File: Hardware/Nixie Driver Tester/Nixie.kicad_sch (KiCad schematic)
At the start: 3 parts, among them J4 Conn_01x04, J5 Conn_01x03, J6 Conn_01x03

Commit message: Initial component layout.
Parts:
- J4: footprint (none) -> Connector_PinHeader_2.54mm:PinHeader_1x04_P2.54mm_Vertical
- J5, J6: footprint (none) -> Connector_PinHeader_2.54mm:PinHeader_1x03_P2.54mm_Vertical
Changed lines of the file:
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@@
 			)
 		)
-		(property "Footprint" ""
+		(property "Footprint" "Connector_PinHeader_2.54mm:PinHeader_1x04_P2.54mm_Vertical"
 			(at 151.13 109.22 0)
 			(effects
@@
 			)
 		)
-		(property "Footprint" ""
+		(property "Footprint" "Connector_PinHeader_2.54mm:PinHeader_1x03_P2.54mm_Vertical"
 			(at 144.78 101.6 0)
 			(effects
@@
 			)
 		)
-		(property "Footprint" ""
+		(property "Footprint" "Connector_PinHeader_2.54mm:PinHeader_1x03_P2.54mm_Vertical"
 			(at 160.02 101.6 0)
 			(effects

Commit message: First reasonable layout.
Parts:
- J4: value Conn_01x04 -> NIX3; footprint Connector_PinHeader_2.54mm:PinHeader_1x04_P2.54mm_Vertical -> Connector_PinSocket_2.54mm:PinSocket_1x04_P2.54mm_Vertical
- J5: value Conn_01x03 -> NIX1; footprint Connector_PinHeader_2.54mm:PinHeader_1x03_P2.54mm_Vertical -> Connector_PinSocket_2.54mm:PinSocket_1x03_P2.54mm_Vertical
- J6: value Conn_01x03 -> NIX2; footprint Connector_PinHeader_2.54mm:PinHeader_1x03_P2.54mm_Vertical -> Connector_PinSocket_2.54mm:PinSocket_1x03_P2.54mm_Vertical
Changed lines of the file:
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@@
 			)
 		)
-		(property "Value" "Conn_01x04"
+		(property "Value" "NIX3"
 			(at 152.4 105.41 90)
 			(effects
@@
 			)
 		)
-		(property "Footprint" "Connector_PinHeader_2.54mm:PinHeader_1x04_P2.54mm_Vertical"
+		(property "Footprint" "Connector_PinSocket_2.54mm:PinSocket_1x04_P2.54mm_Vertical"
 			(at 151.13 109.22 0)
 			(effects
@@
 			)
 		)
-		(property "Value" "Conn_01x03"
+		(property "Value" "NIX1"
 			(at 147.32 102.8699 0)
 			(effects
@@
 			)
 		)
-		(property "Footprint" "Connector_PinHeader_2.54mm:PinHeader_1x03_P2.54mm_Vertical"
+		(property "Footprint" "Connector_PinSocket_2.54mm:PinSocket_1x03_P2.54mm_Vertical"
 			(at 144.78 101.6 0)
 			(effects
@@
 			)
 		)
-		(property "Value" "Conn_01x03"
+		(property "Value" "NIX2"
 			(at 157.48 102.8699 0)
 			(effects
@@
 			)
 		)
-		(property "Footprint" "Connector_PinHeader_2.54mm:PinHeader_1x03_P2.54mm_Vertical"
+		(property "Footprint" "Connector_PinSocket_2.54mm:PinSocket_1x03_P2.54mm_Vertical"
 			(at 160.02 101.6 0)
 			(effects

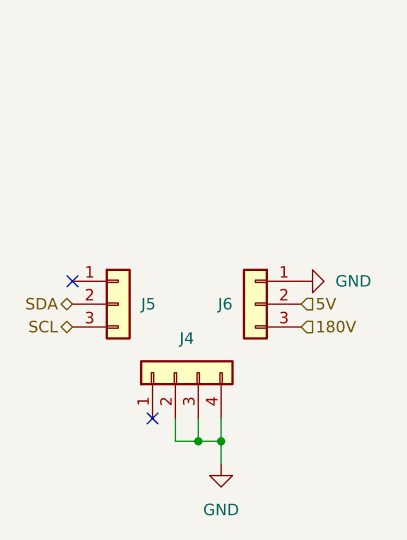
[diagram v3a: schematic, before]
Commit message: Switched to custom nixie driver symbol/footprint
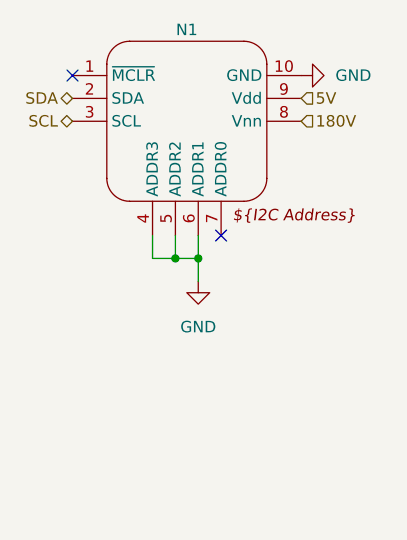
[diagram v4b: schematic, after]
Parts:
- removed J4: NIX3, Connector_PinSocket_2.54mm:PinSocket_1x04_P2.54mm_Vertical, symbol Connector_Generic:Conn_01x04
- removed J5: NIX1, Connector_PinSocket_2.54mm:PinSocket_1x03_P2.54mm_Vertical, symbol Connector_Generic:Conn_01x03
- removed J6: NIX2, Connector_PinSocket_2.54mm:PinSocket_1x03_P2.54mm_Vertical, symbol Connector_Generic:Conn_01x03
- added N1: Nixie, Nixie:Nixie Driver V2, symbol Nixie:Nixie_Driver
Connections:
- net 180V: now also N1.8 (Vnn)
- net 5V: now also N1.9 (Vdd)
- net GND: now also N1.10 (GND), N1.4 (ADDR3), N1.5 (ADDR2), N1.6 (ADDR1)
- net SCL: now also N1.3 (SCL)
- net SDA: now also N1.2 (SDA)
